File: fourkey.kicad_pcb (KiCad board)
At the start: 2 copper layers, 76.5 x 58.9 mm, 6 parts, among them K1 KEYSW, K2 KEYSW, K3 KEYSW, K4 KEYSW, SW1 SW_PUSH, U1 ProMicro

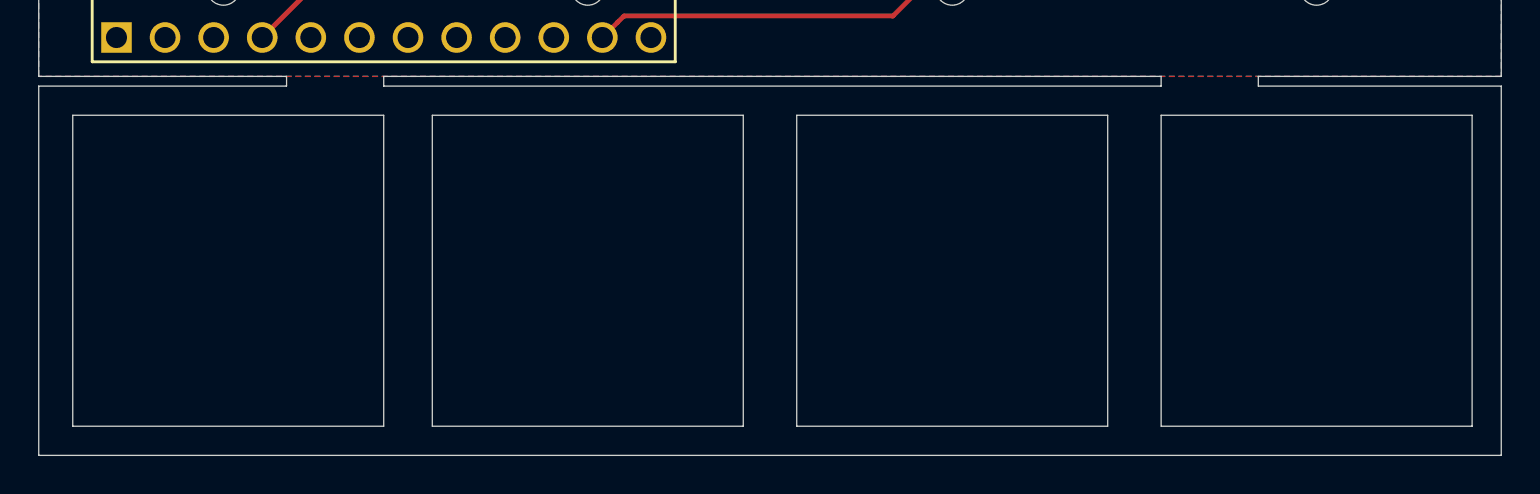
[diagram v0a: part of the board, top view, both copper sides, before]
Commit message: with switch cutouts
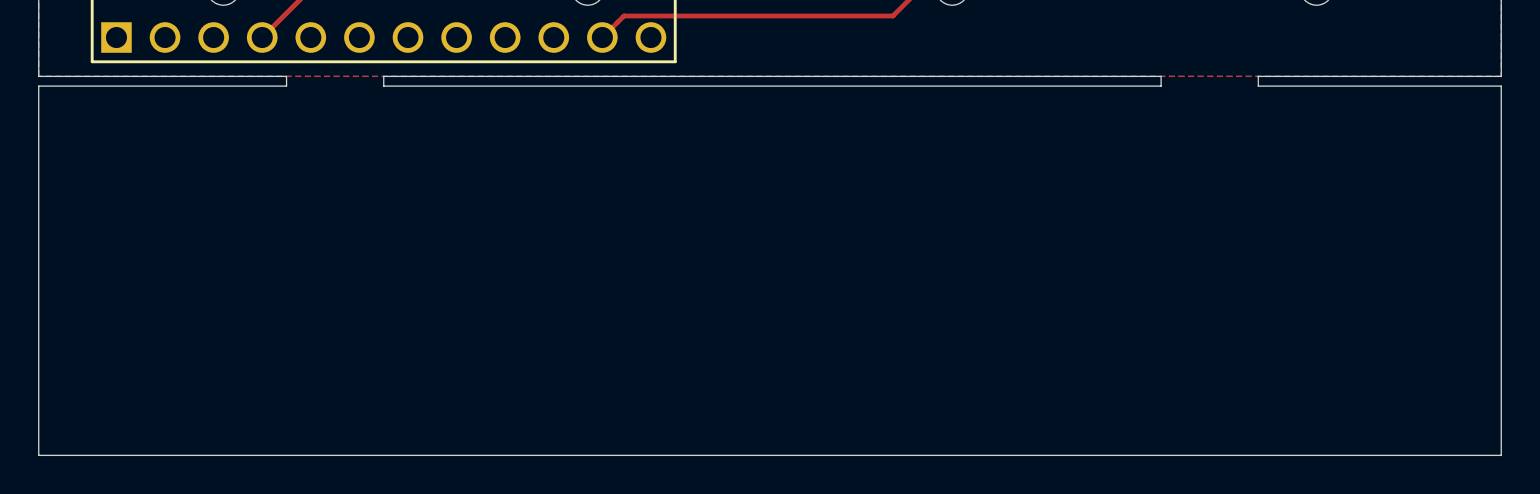
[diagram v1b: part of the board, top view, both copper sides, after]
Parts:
- added REF**: MX_Switch_Cutout, Keebio-Parts:MX_Switch_Cutout, F.Cu at (196.1, 108.0)
- added REF**: MX_Switch_Cutout, Keebio-Parts:MX_Switch_Cutout, F.Cu at (177.0, 108.0)
- added REF**: MX_Switch_Cutout, Keebio-Parts:MX_Switch_Cutout, F.Cu at (158.0, 108.0)
- added REF**: MX_Switch_Cutout, Keebio-Parts:MX_Switch_Cutout, F.Cu at (138.9, 108.0)
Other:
- outline, holes or cut-outs redrawn

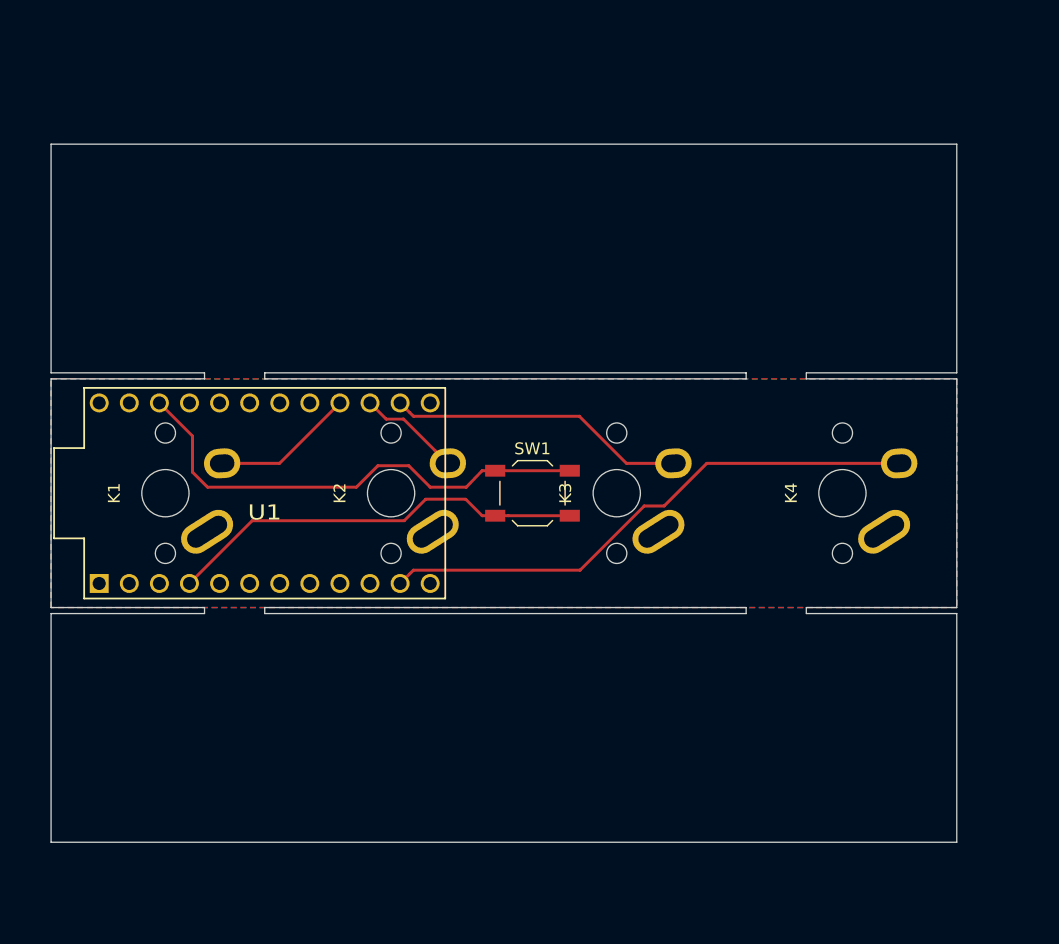
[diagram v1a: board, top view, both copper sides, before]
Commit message: update with pcb plate holes
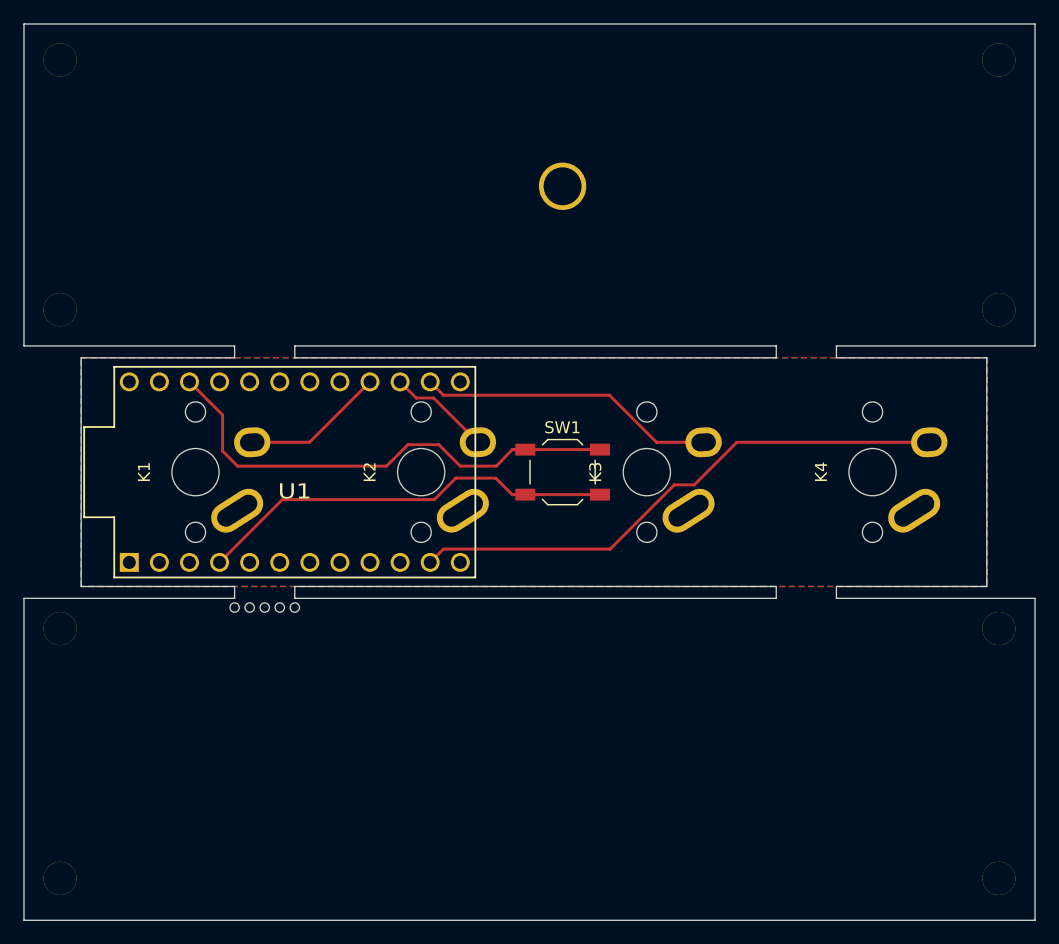
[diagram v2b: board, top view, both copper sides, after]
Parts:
- removed the REF** at (196.1, 108.0)
- removed the REF** at (177.0, 108.0)
- removed the REF** at (158.0, 108.0)
- removed the REF** at (138.9, 108.0)
- added HOLE_M2.6: VAL**, keyboard_parts:HOLE_M2.6, B.Cu at (130.0, 120.7)
- added HOLE_M2.6: VAL**, keyboard_parts:HOLE_M2.6, B.Cu at (209.3, 120.7)
- added HOLE_M2.6: VAL**, keyboard_parts:HOLE_M2.6, B.Cu at (130.0, 99.6)
- added HOLE_M2.6: VAL**, keyboard_parts:HOLE_M2.6, B.Cu at (209.3, 99.6)
- added HOLE_M2.6: VAL**, keyboard_parts:HOLE_M2.6, F.Cu at (130.0, 72.6)
- added HOLE_M2.6: VAL**, keyboard_parts:HOLE_M2.6, F.Cu at (130.0, 51.6)
- added HOLE_M2.6: VAL**, keyboard_parts:HOLE_M2.6, F.Cu at (209.3, 51.6)
- added HOLE_M2.6: VAL**, keyboard_parts:HOLE_M2.6, F.Cu at (209.3, 72.6)
- added HOLE_M3: VAL**, keyboard_parts:HOLE_M3, F.Cu at (172.5, 62.2)
- added REF**: breakaway-mousebites, Keebio-Parts:breakaway-mousebites, F.Cu at (147.3, 98.0)
- added REF**: MX_Switch_Cutout, Keebio-Parts:MX_Switch_Cutout, F.Cu at (198.6, 110.0)
- added REF**: MX_Switch_Cutout, Keebio-Parts:MX_Switch_Cutout, F.Cu at (179.6, 110.0)
- added REF**: MX_Switch_Cutout, Keebio-Parts:MX_Switch_Cutout, F.Cu at (160.5, 110.0)
- added REF**: MX_Switch_Cutout, Keebio-Parts:MX_Switch_Cutout, F.Cu at (141.5, 110.0)
- moved K1 3.10 mm to (141.5, 86.4)
- moved SW1 3.10 mm to (172.5, 86.4)
- moved U1 3.10 mm to (149.9, 86.4)
- moved K2 3.10 mm to (160.5, 86.4)
- moved K3 3.10 mm to (179.6, 86.4)
- moved K4 3.10 mm to (198.6, 86.4)
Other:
- board size 76.5 x 58.9 mm -> 85.3 x 75.7 mm

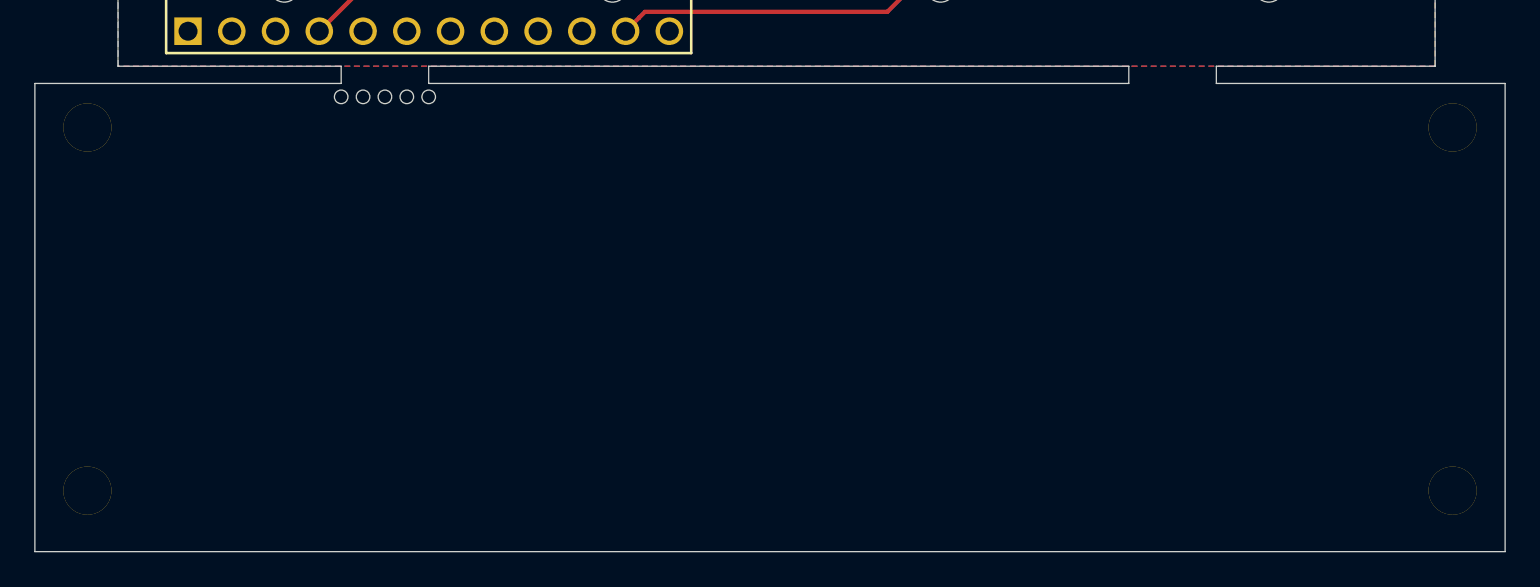
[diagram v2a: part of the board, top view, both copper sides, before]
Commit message: bump down screw holes
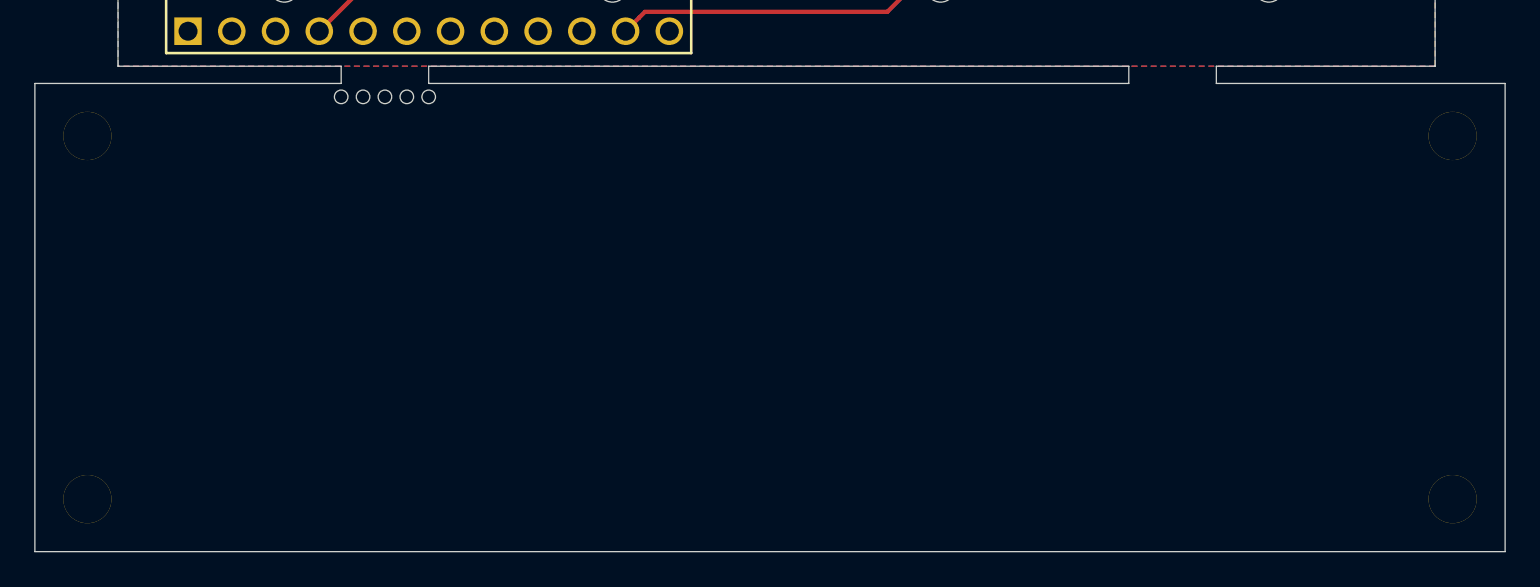
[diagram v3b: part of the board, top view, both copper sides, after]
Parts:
- moved HOLE_M2.6 0.49 mm to (130.0, 100.1)
- moved HOLE_M2.6 0.49 mm to (209.3, 100.1)
- moved HOLE_M2.6 0.49 mm to (130.0, 121.1)
- moved HOLE_M2.6 0.49 mm to (209.3, 121.1)
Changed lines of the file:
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@@
   )
   (module keyboard_parts:HOLE_M2.6 (layer B.Cu)
-    (at 130.048 120.65)
+    (at 130.048 121.142)
     (fp_text reference HOLE_M2.6 (at 0 4.5) (layer B.SilkS) hide
       (effects (font (size 1.524 1.524) (thickness 0.3048)) (justify mirror))
@@
   )
   (module keyboard_parts:HOLE_M2.6 (layer B.Cu)
-    (at 209.296 120.65)
+    (at 209.296 121.142)
     (fp_text reference HOLE_M2.6 (at 0 4.5) (layer B.SilkS) hide
       (effects (font (size 1.524 1.524) (thickness 0.3048)) (justify mirror))
@@
   )
   (module keyboard_parts:HOLE_M2.6 (layer B.Cu)
-    (at 130.048 99.568)
+    (at 130.048 100.06)
     (fp_text reference HOLE_M2.6 (at 0 4.5) (layer B.SilkS) hide
       (effects (font (size 1.524 1.524) (thickness 0.3048)) (justify mirror))
@@
   )
   (module keyboard_parts:HOLE_M2.6 (layer B.Cu)
-    (at 209.296 99.568)
+    (at 209.296 100.06)
     (fp_text reference HOLE_M2.6 (at 0 4.5) (layer B.SilkS) hide
       (effects (font (size 1.524 1.524) (thickness 0.3048)) (justify mirror))

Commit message: bump down switch holes
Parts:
- moved REF** 0.49 mm to (198.6, 110.5)
- moved REF** 0.49 mm to (179.6, 110.5)
- moved REF** 0.49 mm to (160.5, 110.5)
- moved REF** 0.49 mm to (141.5, 110.5)
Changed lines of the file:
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@@
   )
   (module Keebio-Parts:MX_Switch_Cutout locked (layer F.Cu)
-    (at 198.628 109.982 90)
+    (at 198.628 110.474 90)
     (fp_text reference REF** (at 0.25 10.05 90) (layer Eco2.User) hide
       (effects (font (size 1 1) (thickness 0.15)))
@@
   )
   (module Keebio-Parts:MX_Switch_Cutout locked (layer F.Cu)
-    (at 179.578 109.982 90)
+    (at 179.578 110.474 90)
     (fp_text reference REF** (at 0.25 10.05 90) (layer Eco2.User) hide
       (effects (font (size 1 1) (thickness 0.15)))
@@
   )
   (module Keebio-Parts:MX_Switch_Cutout locked (layer F.Cu)
-    (at 160.528 109.982 90)
+    (at 160.528 110.474 90)
     (fp_text reference REF** (at 0.25 10.05 90) (layer Eco2.User) hide
       (effects (font (size 1 1) (thickness 0.15)))
@@
   )
   (module Keebio-Parts:MX_Switch_Cutout locked (layer F.Cu)
-    (at 141.478 109.982 90)
+    (at 141.478 110.474 90)
     (fp_text reference REF** (at 0.25 10.05 90) (layer Eco2.User) hide
       (effects (font (size 1 1) (thickness 0.15)))

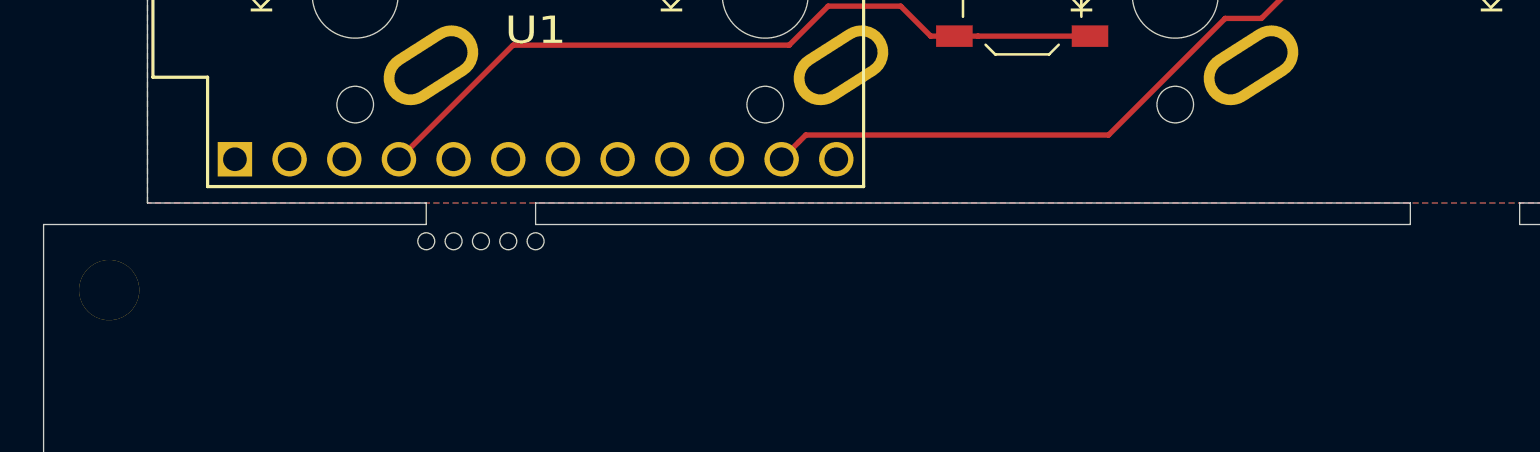
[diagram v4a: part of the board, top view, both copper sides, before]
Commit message: adjust mousebites
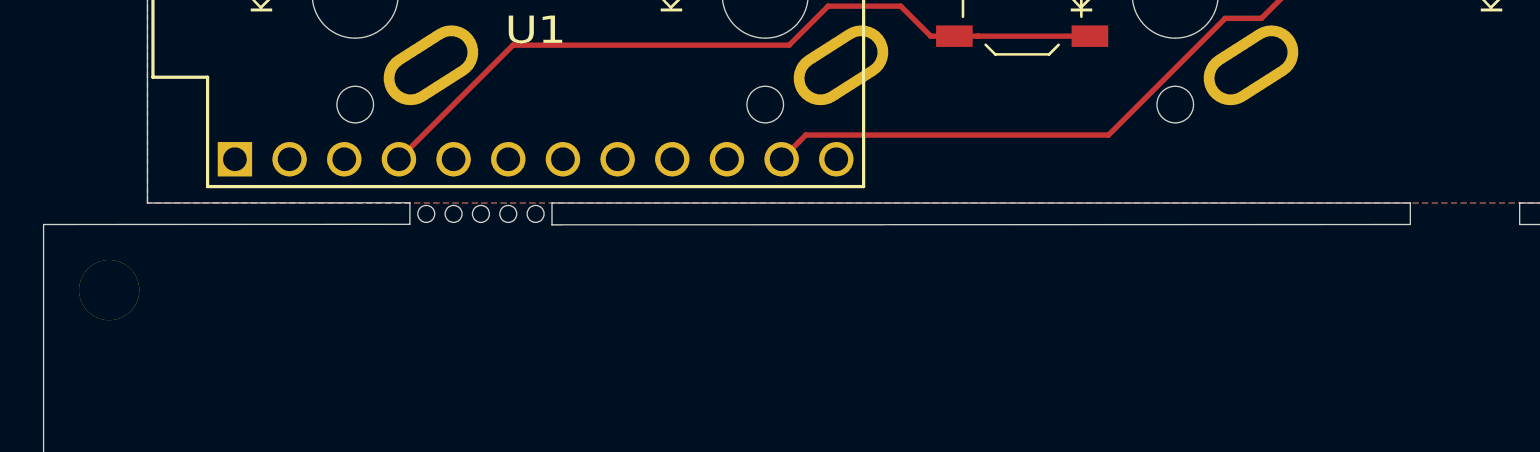
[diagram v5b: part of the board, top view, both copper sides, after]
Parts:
- moved REF** 1.27 mm to (147.3, 96.8)
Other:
- outline, holes or cut-outs redrawn
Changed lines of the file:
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@@
   (general
     (thickness 1.6)
-    (drawings 38)
+    (drawings 35)
     (tracks 38)
     (zones 0)
@@
   (page A4)
   (layers
-    (0 F.Cu signal)
-    (31 B.Cu signal)
+    (0 F.Cu signal hide)
+    (31 B.Cu signal hide)
     (32 B.Adhes user)
     (33 F.Adhes user)
@@
   )
   (module Keebio-Parts:breakaway-mousebites (layer F.Cu)
-    (at 147.32 98.044)
+    (at 147.32 96.774)
     (fp_text reference REF** (at 0 -3.048) (layer Dwgs.User) hide
       (effects (font (size 1 1) (thickness 0.15)))
@@
   (gr_line (start 190.5 96.012) (end 190.5 97.012) (layer Edge.Cuts) (width 0.05))
   (gr_line (start 190.5 96.52) (end 190.5 96.52) (layer Edge.Cuts) (width 0.05))
-  (gr_line (start 127 97.012) (end 144.78 97.012) (layer Edge.Cuts) (width 0.05))
+  (gr_line (start 127 97.012) (end 144.018 97.004) (layer Edge.Cuts) (width 0.05))
   (gr_line (start 127 97.012) (end 127 124.19) (layer Edge.Cuts) (width 0.05))
-  (gr_line (start 149.86 96.012) (end 149.86 97.012) (layer Edge.Cuts) (width 0.05))
-  (gr_line (start 149.86 96.52) (end 149.86 96.52) (layer Edge.Cuts) (width 0.05))
+  (gr_line (start 150.622 96.012) (end 150.622 97.028) (layer Edge.Cuts) (width 0.05))
   (gr_line (start 195.58 96.012) (end 195.58 97.012) (layer Edge.Cuts) (width 0.05))
   (gr_line (start 195.58 97.012) (end 212.344 97.012) (layer Edge.Cuts) (width 0.05))
-  (gr_line (start 144.78 96.012) (end 144.78 97.012) (layer Edge.Cuts) (width 0.05))
-  (gr_line (start 149.86 97.012) (end 190.5 97.012) (layer Edge.Cuts) (width 0.05))
-  (gr_line (start 149.86 96.52) (end 149.86 96.52) (layer Edge.Cuts) (width 0.05))
+  (gr_line (start 144.018 96.004) (end 144.018 97.004) (layer Edge.Cuts) (width 0.05))
+  (gr_line (start 150.622 97.028) (end 190.5 97.012) (layer Edge.Cuts) (width 0.05))
   (gr_line (start 195.58 96.52) (end 195.58 96.52) (layer Edge.Cuts) (width 0.05))
   (gr_line (start 195.58 96.012) (end 208.28 96.012) (layer Edge.Cuts) (width 0.05))
-  (gr_line (start 149.86 96.012) (end 190.5 96.012) (layer Edge.Cuts) (width 0.05))
-  (gr_line (start 144.78 96.012) (end 144.78 96.012) (layer Edge.Cuts) (width 0.05))
+  (gr_line (start 150.622 96.012) (end 190.5 96.012) (layer Edge.Cuts) (width 0.05))
   (gr_line (start 195.58 75.708) (end 195.58 76.708) (layer Edge.Cuts) (width 0.05))
   (gr_line (start 190.5 75.708) (end 190.5 76.708) (layer Edge.Cuts) (width 0.05))
@@
   (gr_line (start 212.344 75.708) (end 212.344 48.53) (layer Edge.Cuts) (width 0.05))
   (gr_line (start 208.28 96.012) (end 208.28 76.708) (layer Edge.Cuts) (width 0.05))
-  (gr_line (start 131.826 96.012) (end 144.78 96.012) (layer Edge.Cuts) (width 0.05))
+  (gr_line (start 131.826 96.012) (end 144.018 96.004) (layer Edge.Cuts) (width 0.05))
   (gr_line (start 131.826 76.708) (end 131.826 96.012) (layer Edge.Cuts) (width 0.05))
   (gr_line (start 208.28 76.708) (end 195.58 76.708) (layer Edge.Cuts) (width 0.05))
